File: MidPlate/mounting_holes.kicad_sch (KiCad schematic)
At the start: 5 parts

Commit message: added PTH's for cap holders and shell
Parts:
- added H14, H15, H16, H17, H18, H19, H20, H21, H22, H23, H24, H25, H26, H27, H28, H29: MountingHoleM2.5NoThread, bots:MountingHole_2.7mm_M2.5_DIN965_Pad, symbol bots:MountingHoleM2.5NoThread

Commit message: midplate changes, ready for order
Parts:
- removed H12, H13: SideMountingHole, bots:MountingHole_3.3mm_M4, symbol bots:SideMountingHole
- added H30, H31, H32, H33, H34, H35, H36, H37, H38, H39, H40, H41, H42, H43, H44, H45, H46, H47, H48, H49, H50: MountingHoleM2.5NoThread, bots:MountingHole_2.7mm_M2.5_DIN965_Pad, symbol bots:MountingHoleM2.5NoThread

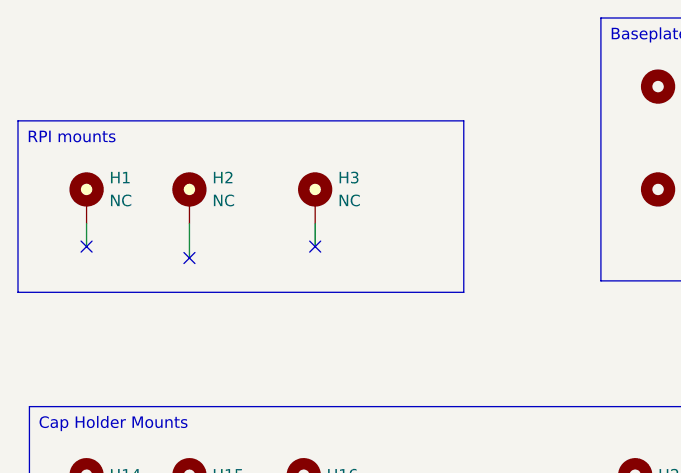
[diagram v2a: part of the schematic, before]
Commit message: midplate 5V buck converter
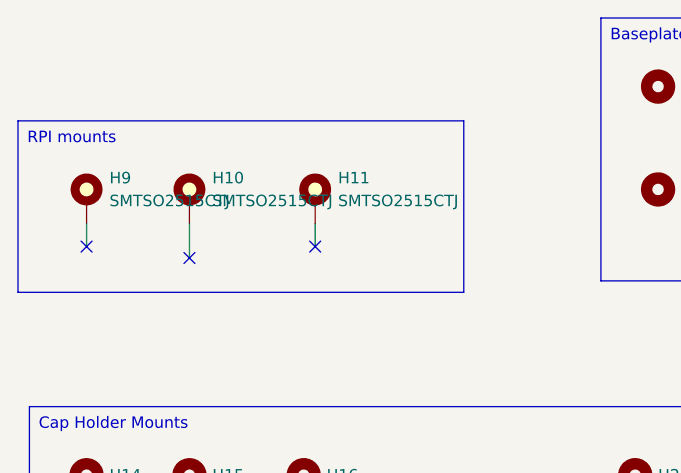
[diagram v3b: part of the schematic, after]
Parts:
- removed H1, H2, H3: NC, bots:Keystone_24929, symbol bots:ZeroH_Keystone24929_Pad
- added H10, H11, H9: SMTSO2515CTJ, bots:SMTSO2515CTJ, symbol bots:SMTSO2515CTJ

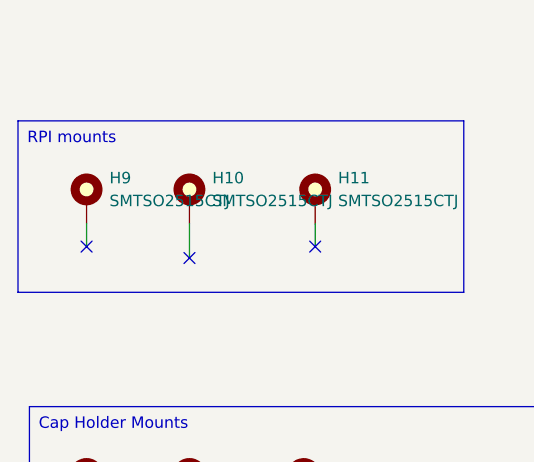
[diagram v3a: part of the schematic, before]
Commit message: power board and midplate updates (mostly finalized)
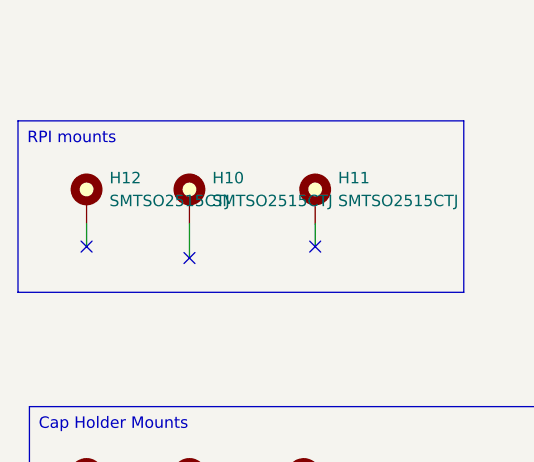
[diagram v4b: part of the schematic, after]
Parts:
- renumbered H9 to H12
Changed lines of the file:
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@@
   (symbol (lib_id "bots:SMTSO2515CTJ") (at 55.88 64.77 0) (unit 1)
     (in_bom yes) (on_board yes) (dnp no) (fields_autoplaced)
-    (property "Reference" "H9" (at 58.42 62.23 0)
+    (property "Reference" "H12" (at 58.42 62.23 0)
       (effects (font (size 1.27 1.27)) (justify left))
     )
@@
       (project "midplate"
         (path "/69058343-dac8-421b-a3f6-e069eb1ba8ae/dd4f1e83-2671-4cd9-8990-217fc355ed24"
-          (reference "H9") (unit 1)
+          (reference "H12") (unit 1)
         )
       )

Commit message: midplate
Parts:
- H10, H11, H12: value SMTSO2515CTJ -> RPI
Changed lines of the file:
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@@
       (effects (font (size 1.27 1.27)) (justify left))
     )
-    (property "Value" "SMTSO2515CTJ" (at 69.85 64.77 0)
-      (effects (font (size 1.27 1.27)) (justify left))
+    (property "Value" "RPI" (at 69.85 64.77 0)
+      (effects (font (size 1.27 1.27)) (justify left) hide)
     )
     (property "Footprint" "bots:SMTSO2515CTJ" (at 67.31 64.77 0)
@@
       (effects (font (size 1.27 1.27)) (justify left))
     )
-    (property "Value" "SMTSO2515CTJ" (at 83.82 64.77 0)
-      (effects (font (size 1.27 1.27)) (justify left))
+    (property "Value" "RPI" (at 83.82 64.77 0)
+      (effects (font (size 1.27 1.27)) (justify left) hide)
     )
     (property "Footprint" "bots:SMTSO2515CTJ" (at 81.28 64.77 0)
@@
       (effects (font (size 1.27 1.27)) (justify left))
     )
-    (property "Value" "SMTSO2515CTJ" (at 58.42 64.77 0)
-      (effects (font (size 1.27 1.27)) (justify left))
+    (property "Value" "RPI" (at 58.42 64.77 0)
+      (effects (font (size 1.27 1.27)) (justify left) hide)
     )
     (property "Footprint" "bots:SMTSO2515CTJ" (at 55.88 64.77 0)

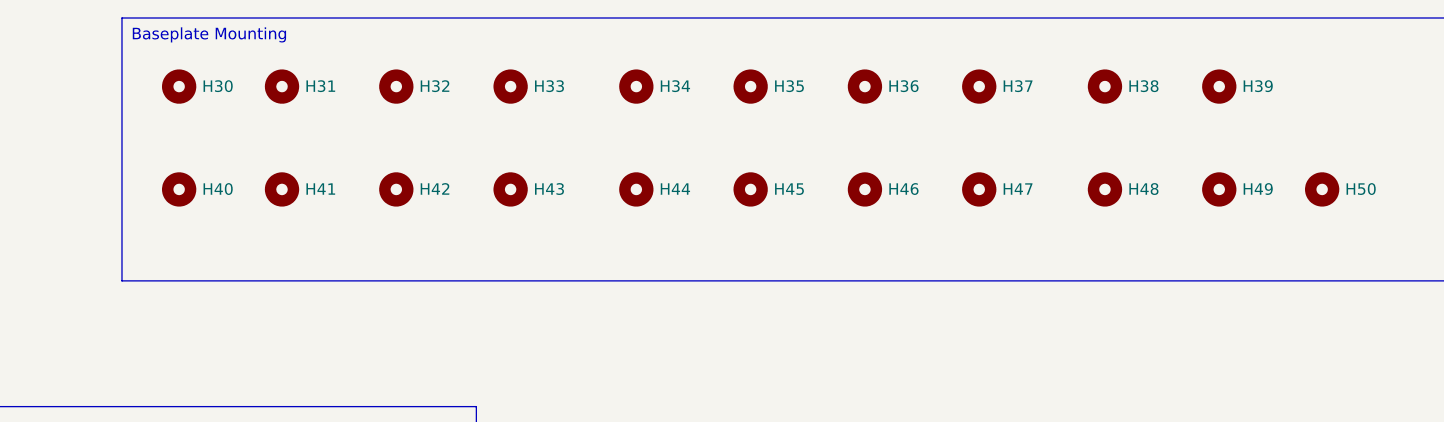
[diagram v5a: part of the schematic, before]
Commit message: midplate + chicker bom
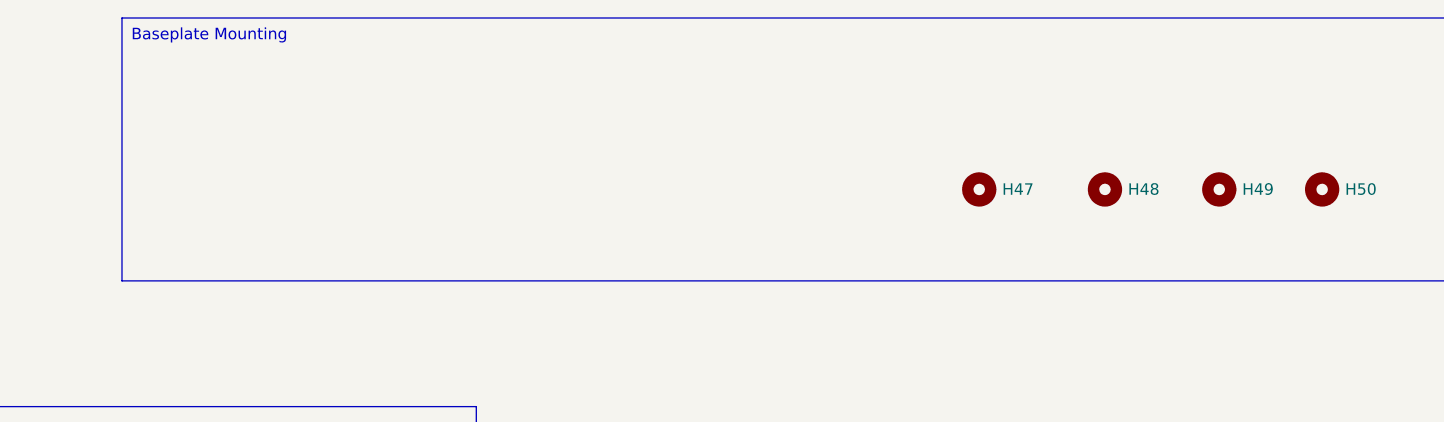
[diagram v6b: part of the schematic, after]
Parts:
- removed H30, H31, H32, H33, H34, H35, H36, H37, H38, H39, H40, H41, H42, H43, H44, H45, H46: MountingHoleM2.5NoThread, bots:MountingHole_2.7mm_M2.5_DIN965_Pad, symbol bots:MountingHoleM2.5NoThread

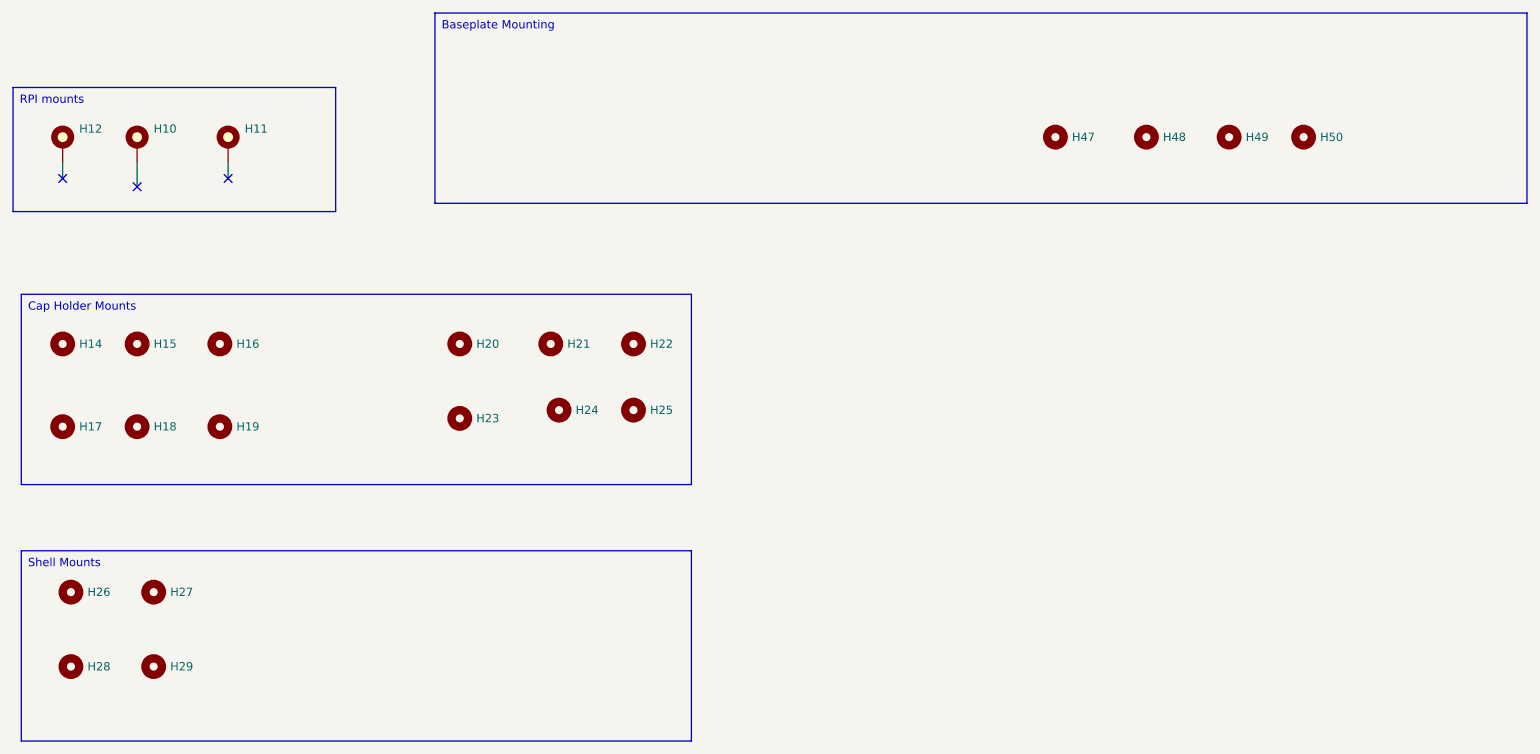
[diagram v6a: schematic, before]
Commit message: feat: add midplate and shell mounting
- Reduce PCB Diameter to 174mm
- Add cutouts for shell mounting
- Reduce cap holder screw holes from 6 to 4
- Rotate power switch 30 deg towards edge
- Add holes for midplate mounting
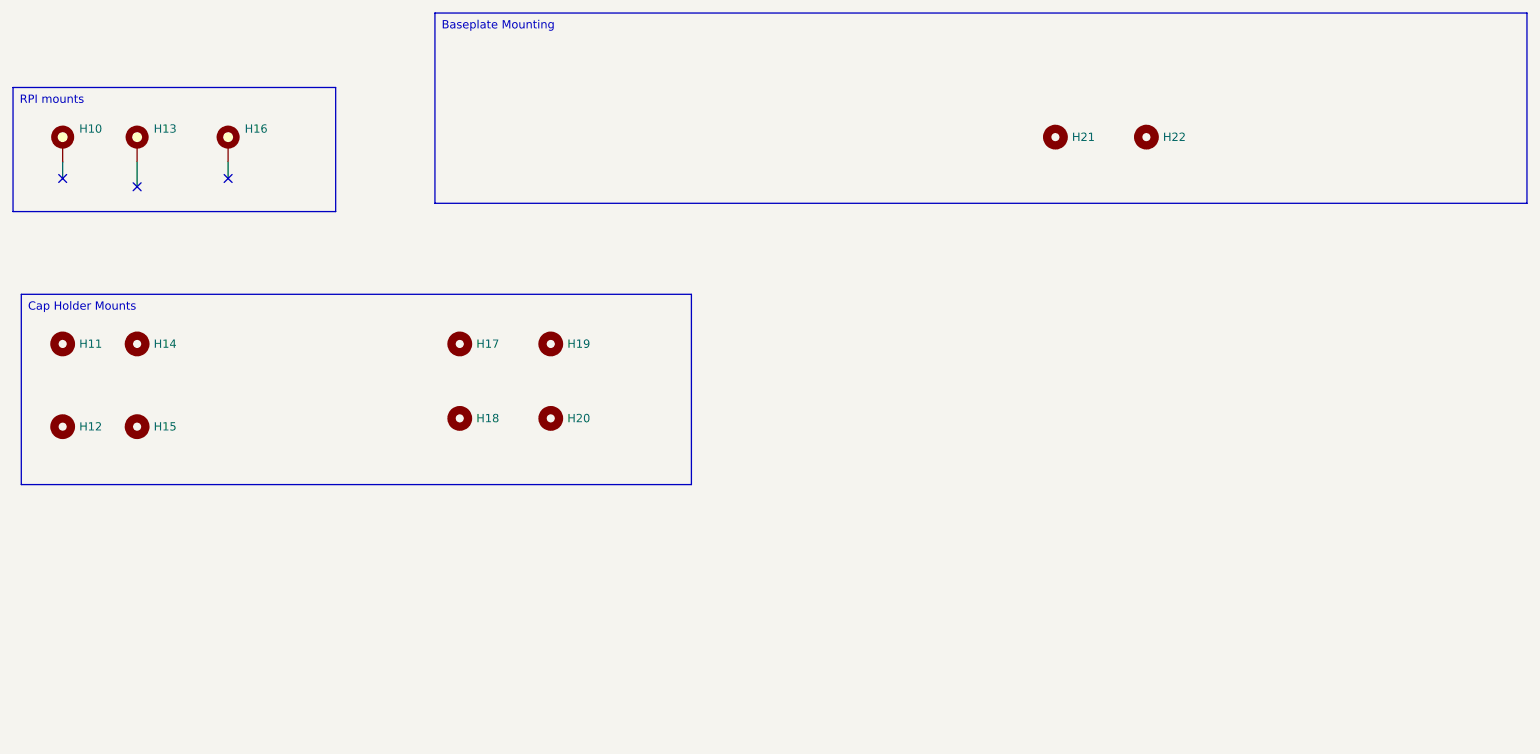
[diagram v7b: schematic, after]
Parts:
- removed H16, H17, H22, H23, H26, H27, H28, H29, H49, H50: MountingHoleM2.5NoThread, bots:MountingHole_2.7mm_M2.5_DIN965_Pad, symbol bots:MountingHoleM2.5NoThread
- renumbered H12 to H10, H14 to H11, H18 to H12, H10 to H13, H15 to H14, H19 to H15, H11 to H16, H20 to H17, H24 to H18, H21 to H19, H25 to H20, H47 to H21, H48 to H22
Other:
- moved on the sheet: H12, H15, H18, H20

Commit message: midplate updates
- pretty close to order: need to verify if we can get 2oz outer copper
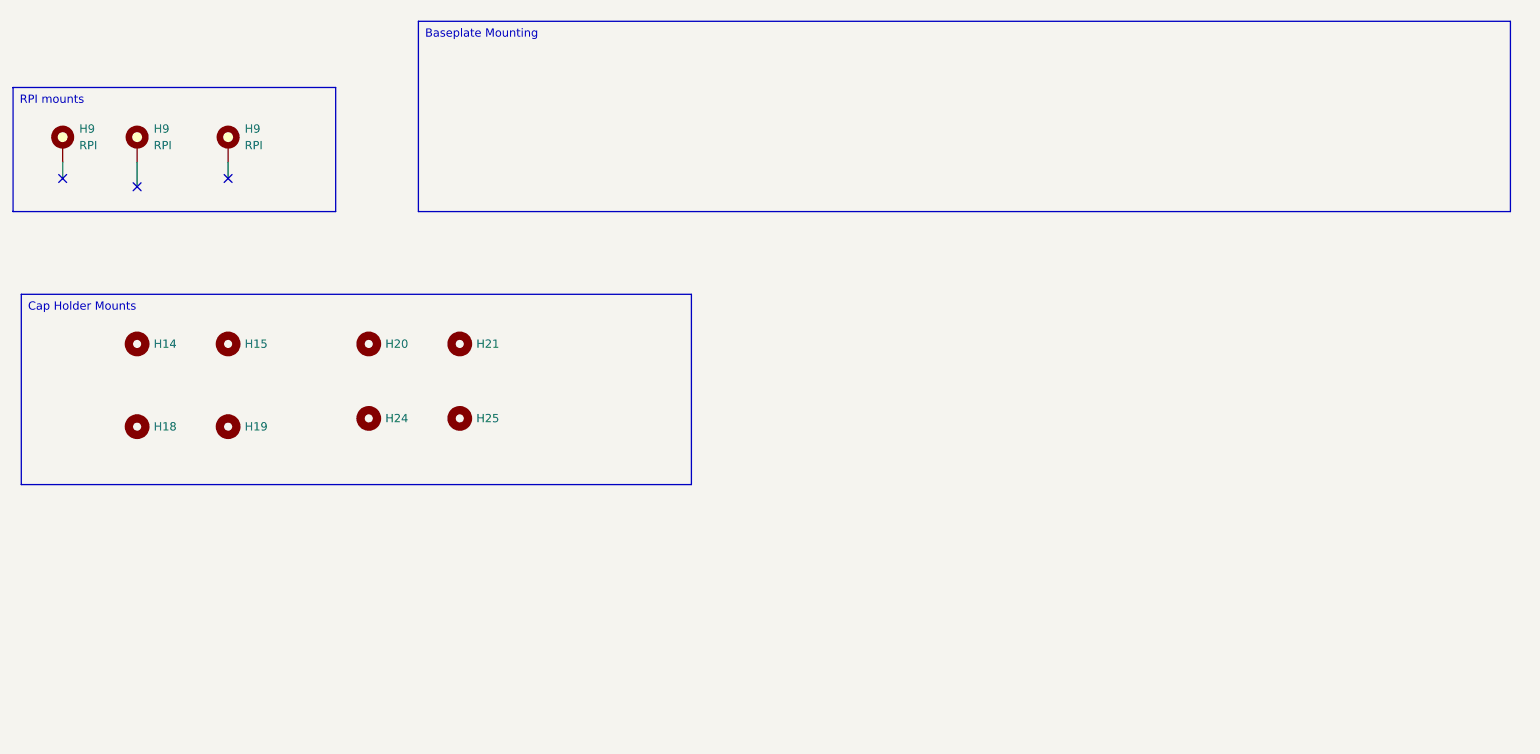
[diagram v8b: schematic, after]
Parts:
- removed H10, H13, H16: RPI, bots:SMTSO2515CTJ, symbol bots:SMTSO2515CTJ
- removed H21, H22: MountingHoleM2.5NoThread, bots:MountingHole_2.7mm_M2.5_DIN965_Pad, symbol bots:MountingHoleM2.5NoThread
- added H9 (x3): RPI, bots:SMTSO2515CTJ, symbol thebots_symlib:SMTSO2515CTJ
- renumbered H11 to H18, H12 to H19, H17 to H21, H19 to H24, H18 to H25
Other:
- moved on the sheet: H15, H18, H19, H20, H24
